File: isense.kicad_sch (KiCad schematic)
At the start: 0 parts

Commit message: Added some text in the subsheets to outline what needs to be added inside of each subsheet
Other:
- note added: "TODO: - Use an error amplifier to measure the amount of current coming in - Use a comparator to determine whether the current being drawn is over the limit set by the Dev Board"
- title: (none) -> Current Sensing
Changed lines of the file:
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@@
 	(paper "A4")
 	(title_block
+		(title "Current Sensing")
 		(date "2024-10-18")
 		(rev "1")
@@
 		(comment 1 "Robomaster")
 	)
+	(text "TODO:\n- Use an error amplifier to measure the amount of current coming in\n- Use a comparator to determine whether the current being drawn is over the limit set by the Dev Board"
+		(exclude_from_sim no)
+		(at 97.155 96.52 0)
+		(effects
+			(font
+				(size 1.27 1.27)
+			)
+			(justify left top)
+		)
+	)
 )

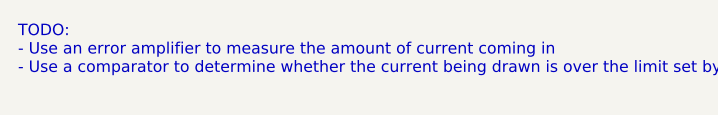
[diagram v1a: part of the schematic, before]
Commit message: Added two more subsheets and updated all text inside
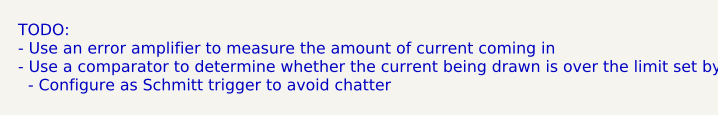
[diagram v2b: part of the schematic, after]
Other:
- note added: "TODO: - Use an error amplifier to measure the amount of current coming in - Use a comparator to determine whether the current being drawn is over the limit set by the Dev Board - Configure as Schmitt trigger to avoid chatter"
- note removed: "TODO: - Use an error amplifier to measure the amount of current coming in - Use a comparator to determine whether the current being drawn is over the limit set by the Dev Board"
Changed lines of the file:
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@@
 		(comment 1 "Robomaster")
 	)
-	(text "TODO:\n- Use an error amplifier to measure the amount of current coming in\n- Use a comparator to determine whether the current being drawn is over the limit set by the Dev Board"
+	(text "TODO:\n- Use an error amplifier to measure the amount of current coming in\n- Use a comparator to determine whether the current being drawn is over the limit set by the Dev Board\n  - Configure as Schmitt trigger to avoid chatter"
 		(exclude_from_sim no)
 		(at 97.155 96.52 0)

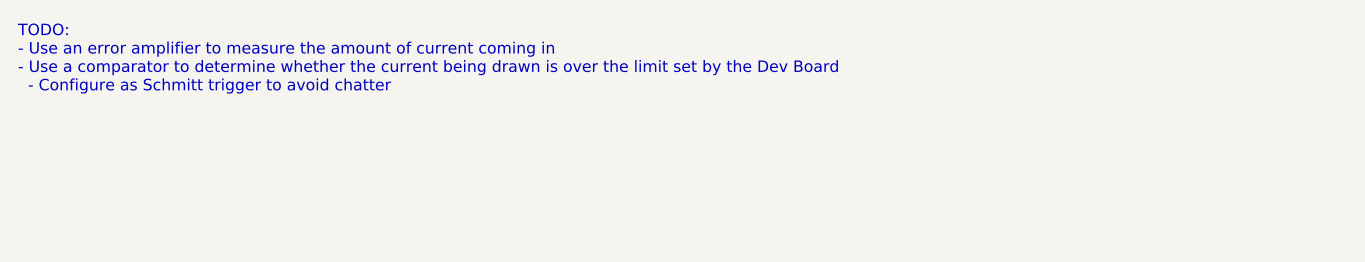
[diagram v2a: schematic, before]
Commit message: Added in & out data from each subsheet
For more details, please contact @leftisttachyon on Discord
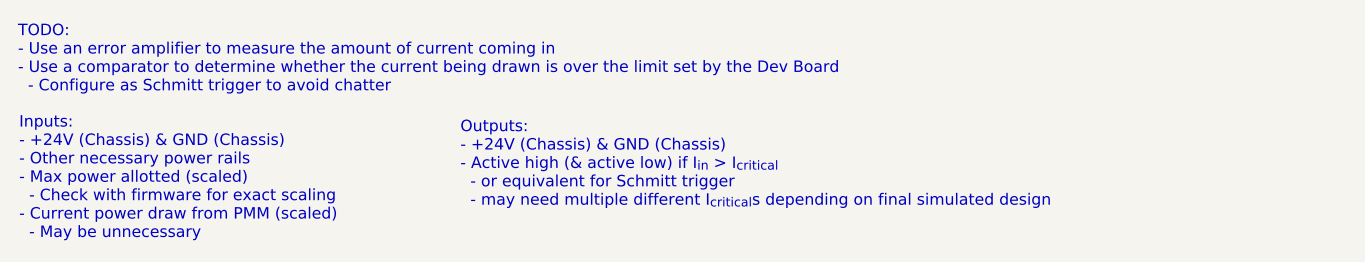
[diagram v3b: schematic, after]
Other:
- note added: "Inputs: - +24V (Chassis) & GND (Chassis) - Other necessary power rails - Max power allotted (scaled) - Check with firmware for exact scaling - Current power draw from PMM (scaled) - May be unnecessary"
- note added: "Outputs: - +24V (Chassis) & GND (Chassis) - Active high (& active low) if I_{in} > I_{critical} - or equivalent for Schmitt trigger - may need multiple different I_{critical}s depending on final simulated design"
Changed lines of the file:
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@@
 		(comment 1 "Robomaster")
+	)
+	(text "Inputs:\n- +24V (Chassis) & GND (Chassis)\n- Other necessary power rails\n- Max power allotted (scaled)\n  - Check with firmware for exact scaling\n- Current power draw from PMM (scaled)\n  - May be unnecessary"
+		(exclude_from_sim no)
+		(at 97.282 106.68 0)
+		(effects
+			(font
+				(size 1.27 1.27)
+			)
+			(justify left top)
+		)
+	)
+	(text "Outputs:\n- +24V (Chassis) & GND (Chassis)\n- Active high (& active low) if I_{in} > I_{critical}\n  - or equivalent for Schmitt trigger\n  - may need multiple different I_{critical}s depending on final simulated design"
+		(exclude_from_sim no)
+		(at 146.304 107.188 0)
+		(effects
+			(font
+				(size 1.27 1.27)
+			)
+			(justify left top)
+		)
 	)
 	(text "TODO:\n- Use an error amplifier to measure the amount of current coming in\n- Use a comparator to determine whether the current being drawn is over the limit set by the Dev Board\n  - Configure as Schmitt trigger to avoid chatter"

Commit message: Completed first version of housekeeping supplies
+5V and +3V3 from mini PC +24V
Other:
- company: UT Stampede -> UT Robomaster
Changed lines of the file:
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@@
 	(title_block
 		(title "Current Sensing")
-		(date "2024-10-18")
+		(date "2024-11-15")
 		(rev "1")
-		(company "UT Stampede")
+		(company "UT Robomaster")
 		(comment 1 "Robomaster")
 	)

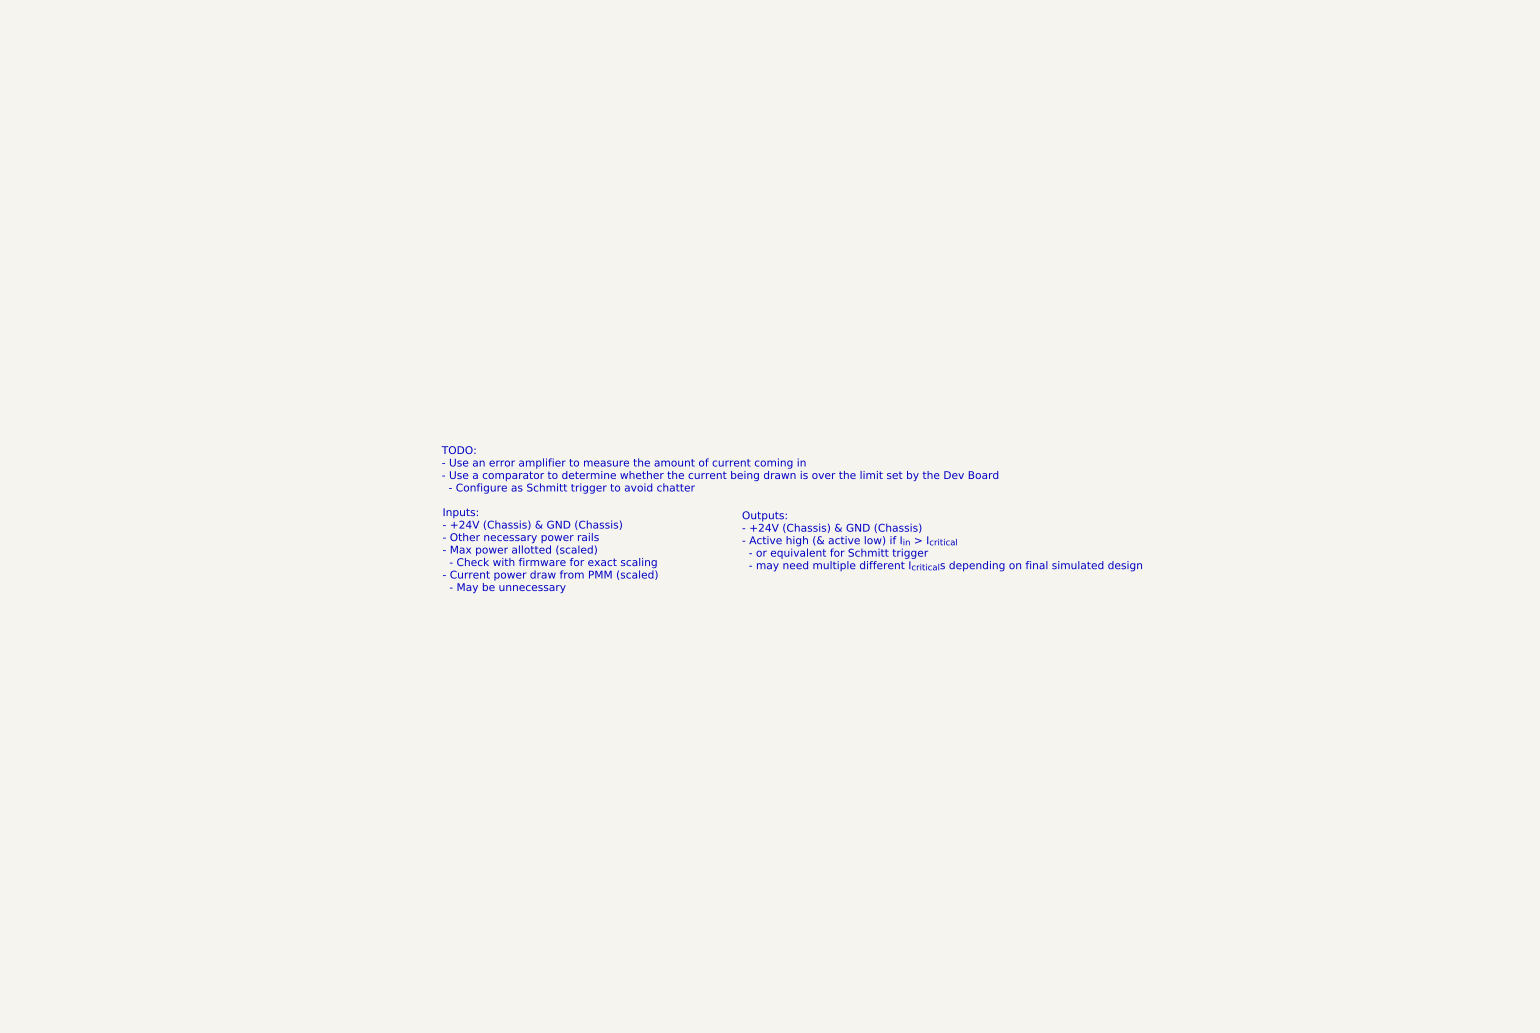
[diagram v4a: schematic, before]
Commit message: added isense
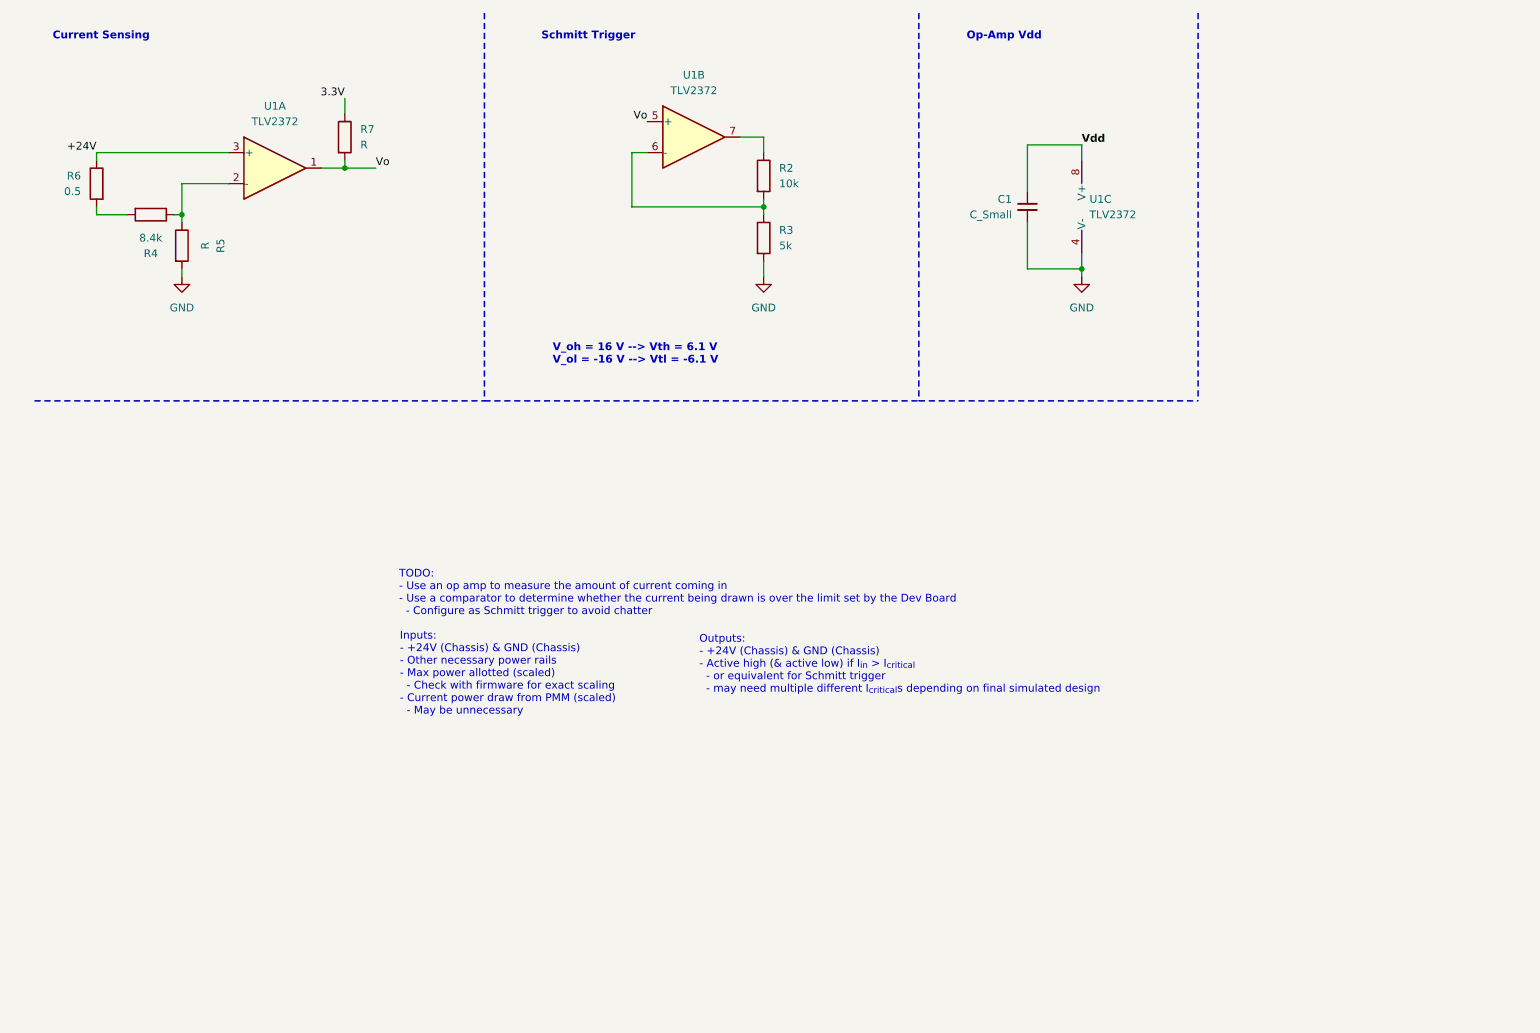
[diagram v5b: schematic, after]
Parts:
- added C1: C_Small, symbol Device:C_Small
- added R2: 10k, symbol Device:R
- added R3: 5k, symbol Device:R
- added R4: 8.4k, symbol Device:R
- added R5, R7: R, symbol Device:R
- added R6: 0.5, symbol Device:R
- added U1: TLV2372, symbol Amplifier_Operational:TLV2372
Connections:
- new net: R2.1, U1.7
- new net: R2.2, R3.1, U1.6 (-)
- new net: R4.2, R6.2
- new net: R4.1, R5.1, U1.2 (-)
- new net +24V: R6.1, U1.3 (+)
- new net 3.3V: R7.1
- new net GND: C1.2, R3.2, R5.2, U1.4 (V-)
- new net Vdd: C1.1, U1.8 (V+)
- new net Vo: R7.2, U1.1, U1.5 (+)
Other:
- note added: "Current Sensing"
- note added: "Op-Amp Vdd"
- note added: "Schmitt Trigger"
- note added: "TODO: - Use an op amp to measure the amount of current coming in - Use a comparator to determine whether the current being drawn is over the limit set by the Dev Board - Configure as Schmitt trigger to avoid chatter"
- note added: "V_oh = 16 V --> Vth = 6.1 V V_ol = -16 V --> Vtl = -6.1 V"
- note removed: "TODO: - Use an error amplifier to measure the amount of current coming in - Use a comparator to determine whether the current being drawn is over the limit set by the Dev Board - Configure as Schmitt trigger to avoid chatter"

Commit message: Trying to do current sense but it's not fun
canercanercnarennc
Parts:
- added R12: 0.02, Resistor_SMD:R_0805_2012Metric_Pad1.20x1.40mm_HandSolder, symbol Device:R
- added R13: 100k, Resistor_SMD:R_0603_1608Metric_Pad0.98x0.95mm_HandSolder, symbol Device:R
- added U7: INA138, Package_TO_SOT_SMD:SOT-23_Handsoldering, symbol Amplifier_Current:INA138
- added U8: LM2904, Package_SO:SOIC-8_3.9x4.9mm_P1.27mm, symbol Amplifier_Operational:LM2904
- added U9: LM393, Package_SO:SOIC-8_3.9x4.9mm_P1.27mm, symbol Comparator:LM393
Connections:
- new net CURR: U8.1, U8.2 (-), U9.2 (-), U9.6 (-)
- new net CURR_{RAW}: R13.1, U7.1, U8.3 (+)
- new net GNDPWR: R13.2, U7.2 (GND), U9.4 (V-)
- new net PWR_{IN}: R12.1, U7.3 (+), U7.5 (V+)
- new net PWR_{OUT}: R12.2, U7.4 (-)
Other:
- note added: "(Must be buffered before being read into ADC)"
- note added: "100kΩ = 20x amplification = ~2V of swing (0-120W)"
- note added: "Buffering"
- note added: "Charging enable V_{TH} (~105W) = 1.7500V V_{TL} (~100W) = 1.6667V"
- note added: "Current sensing"
- note added: "Direct drive enable V_{TH} (~115W) = 1.9167V V_{TL} (~110W) = 1.8333V"
- note added: "R_{S} chosen such that the max current of 5A (@120W) is 100mV"
- note added: "To isolate from input impedances"

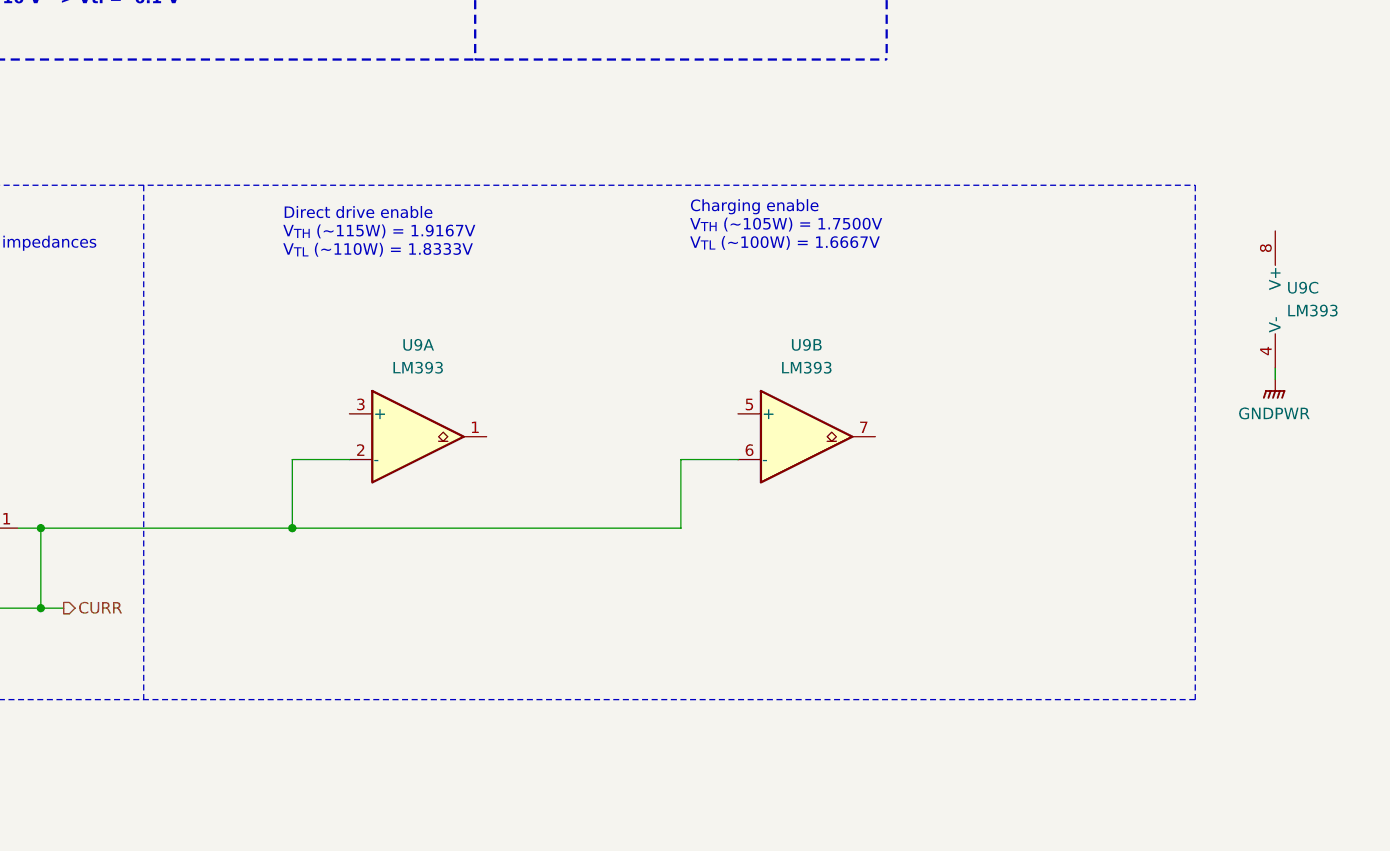
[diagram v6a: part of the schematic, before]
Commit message: Completed sense comparators
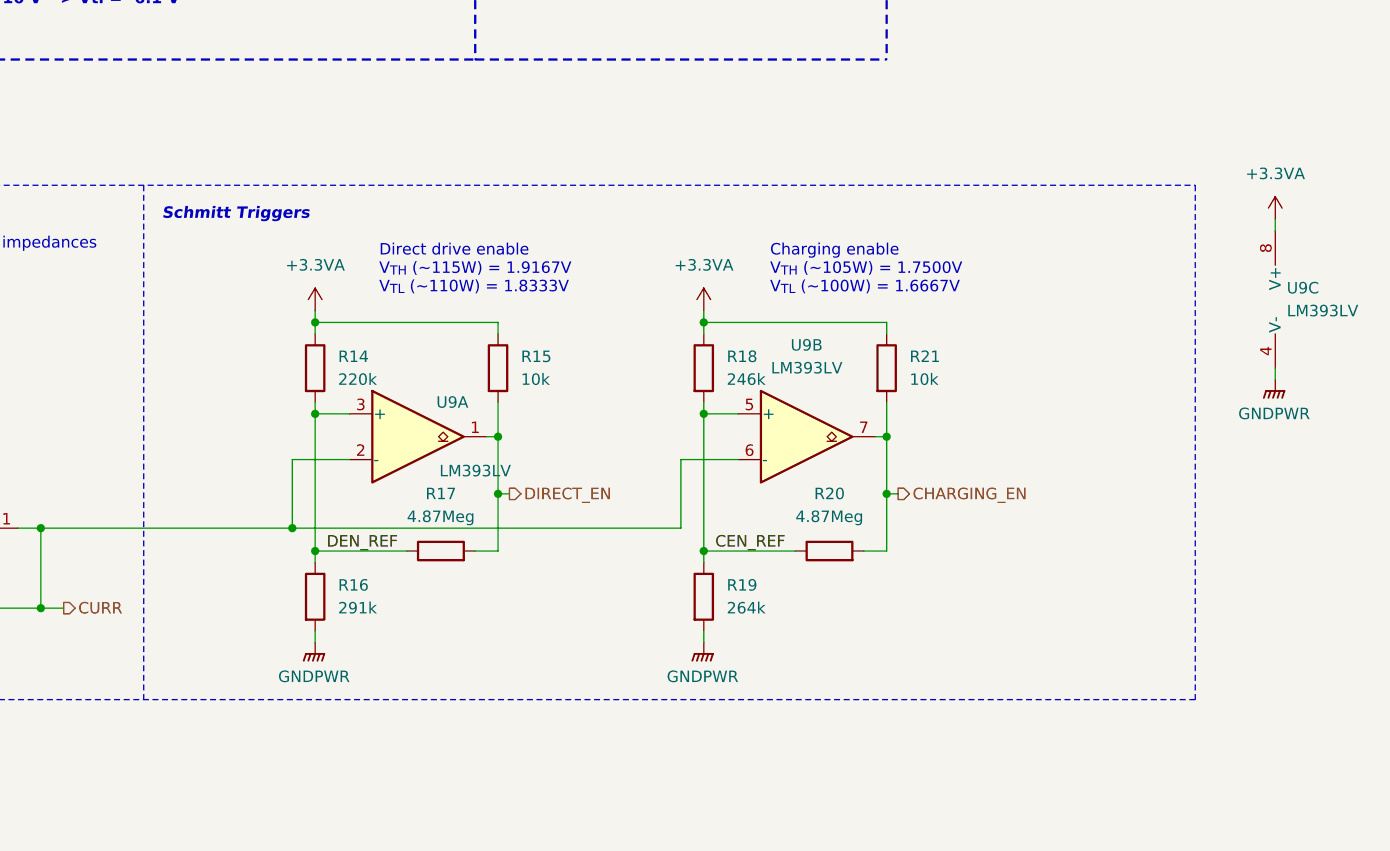
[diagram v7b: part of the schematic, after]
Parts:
- added R14: 220k, Resistor_SMD:R_0603_1608Metric_Pad0.98x0.95mm_HandSolder, symbol Device:R
- added R15, R21: 10k, Resistor_SMD:R_0603_1608Metric_Pad0.98x0.95mm_HandSolder, symbol Device:R
- added R16: 291k, Resistor_SMD:R_0603_1608Metric_Pad0.98x0.95mm_HandSolder, symbol Device:R
- added R17, R20: 4.87Meg, Resistor_SMD:R_0603_1608Metric_Pad0.98x0.95mm_HandSolder, symbol Device:R
- added R18: 246k, Resistor_SMD:R_0603_1608Metric_Pad0.98x0.95mm_HandSolder, symbol Device:R
- added R19: 264k, Resistor_SMD:R_0603_1608Metric_Pad0.98x0.95mm_HandSolder, symbol Device:R
- U9: value LM393 -> LM393LV; symbol Comparator:LM393 -> ! Robomaster:LM393LV
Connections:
- net GNDPWR: now also R16.2, R19.2
- net CEN_REF: now reaches U9.5 (+)
- net CEN_REF: now also R18.2, R19.1, R20.1
- net CHARGING_EN: now reaches U9.7
- net CHARGING_EN: now also R20.2, R21.2
- net +3.3VA: now reaches U9.8 (V+)
- net +3.3VA: now also R14.1, R15.1, R18.1, R21.1
- net DIRECT_EN: now reaches U9.1
- net DIRECT_EN: now also R15.2, R17.2
- net DEN_REF: now reaches U9.3 (+)
- net DEN_REF: now also R14.2, R16.1, R17.1
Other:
- note added: "Schmitt Triggers"
